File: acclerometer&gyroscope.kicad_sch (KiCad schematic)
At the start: 5 parts, among them U11 LSM6DS3

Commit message: PCB routing
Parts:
- renumbered C39 to C41, C40 to C42
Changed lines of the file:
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@@
 	(title_block
 		(title "3D Accelerometer & 3D Gyroscope")
-		(date "2025-11-26")
+		(date "2025-12-01")
 		(rev "v0.0")
 		(company "TJ71PL")
@@
 		(dnp no)
 		(fields_autoplaced yes)
-		(property "Reference" "#PWR086"
+		(property "Reference" "#PWR088"
 			(at 166.37 91.44 0)
 			(effects
@@
 			(project "Precision Clock"
 				(path "/c9a8ff63-a0d1-4125-9dd1-40fb53daf536/83e9a93f-b32e-4175-81a6-6f58261db903"
-					(reference "#PWR086")
+					(reference "#PWR088")
 					(unit 1)
 				)
@@
 		(dnp no)
 		(fields_autoplaced yes)
-		(property "Reference" "#PWR082"
+		(property "Reference" "#PWR084"
 			(at 128.27 73.66 0)
 			(effects
@@
 			(project "Precision Clock"
 				(path "/c9a8ff63-a0d1-4125-9dd1-40fb53daf536/83e9a93f-b32e-4175-81a6-6f58261db903"
-					(reference "#PWR082")
+					(reference "#PWR084")
 					(unit 1)
 				)
@@
 		(dnp no)
 		(fields_autoplaced yes)
-		(property "Reference" "C40"
+		(property "Reference" "C42"
 			(at 116.84 77.4699 0)
 			(effects
@@
 			(project "Precision Clock"
 				(path "/c9a8ff63-a0d1-4125-9dd1-40fb53daf536/83e9a93f-b32e-4175-81a6-6f58261db903"
-					(reference "C40")
+					(reference "C42")
 					(unit 1)
 				)
@@
 		(dnp no)
 		(fields_autoplaced yes)
-		(property "Reference" "#PWR081"
+		(property "Reference" "#PWR083"
 			(at 113.03 91.44 0)
 			(effects
@@
 			(project "Precision Clock"
 				(path "/c9a8ff63-a0d1-4125-9dd1-40fb53daf536/83e9a93f-b32e-4175-81a6-6f58261db903"
-					(reference "#PWR081")
+					(reference "#PWR083")
 					(unit 1)
 				)
@@
 		(dnp no)
 		(fields_autoplaced yes)
-		(property "Reference" "#PWR085"
+		(property "Reference" "#PWR087"
 			(at 158.75 121.92 0)
 			(effects
@@
 			(project "Precision Clock"
 				(path "/c9a8ff63-a0d1-4125-9dd1-40fb53daf536/83e9a93f-b32e-4175-81a6-6f58261db903"
-					(reference "#PWR085")
+					(reference "#PWR087")
 					(unit 1)
 				)
@@
 		(dnp no)
 		(fields_autoplaced yes)
-		(property "Reference" "C39"
+		(property "Reference" "C41"
 			(at 104.14 77.4699 0)
 			(effects
@@
 			(project "Precision Clock"
 				(path "/c9a8ff63-a0d1-4125-9dd1-40fb53daf536/83e9a93f-b32e-4175-81a6-6f58261db903"
-					(reference "C39")
+					(reference "C41")
 					(unit 1)
 				)
@@
 		(dnp no)
 		(fields_autoplaced yes)
-		(property "Reference" "#PWR080"
+		(property "Reference" "#PWR082"
 			(at 100.33 91.44 0)
 			(effects
@@
 			(project "Precision Clock"
 				(path "/c9a8ff63-a0d1-4125-9dd1-40fb53daf536/83e9a93f-b32e-4175-81a6-6f58261db903"
-					(reference "#PWR080")
+					(reference "#PWR082")
 					(unit 1)
 				)
@@
 		(dnp no)
 		(fields_autoplaced yes)
-		(property "Reference" "#PWR083"
+		(property "Reference" "#PWR085"
 			(at 130.81 135.89 0)
 			(effects
@@
 			(project "Precision Clock"
 				(path "/c9a8ff63-a0d1-4125-9dd1-40fb53daf536/83e9a93f-b32e-4175-81a6-6f58261db903"
-					(reference "#PWR083")
+					(reference "#PWR085")
 					(unit 1)
 				)
@@
 		(dnp no)
 		(fields_autoplaced yes)
-		(property "Reference" "#PWR084"
+		(property "Reference" "#PWR086"
 			(at 153.67 105.41 0)
 			(effects
@@
 			(project "Precision Clock"
 				(path "/c9a8ff63-a0d1-4125-9dd1-40fb53daf536/83e9a93f-b32e-4175-81a6-6f58261db903"
-					(reference "#PWR084")
+					(reference "#PWR086")
 					(unit 1)
 				)

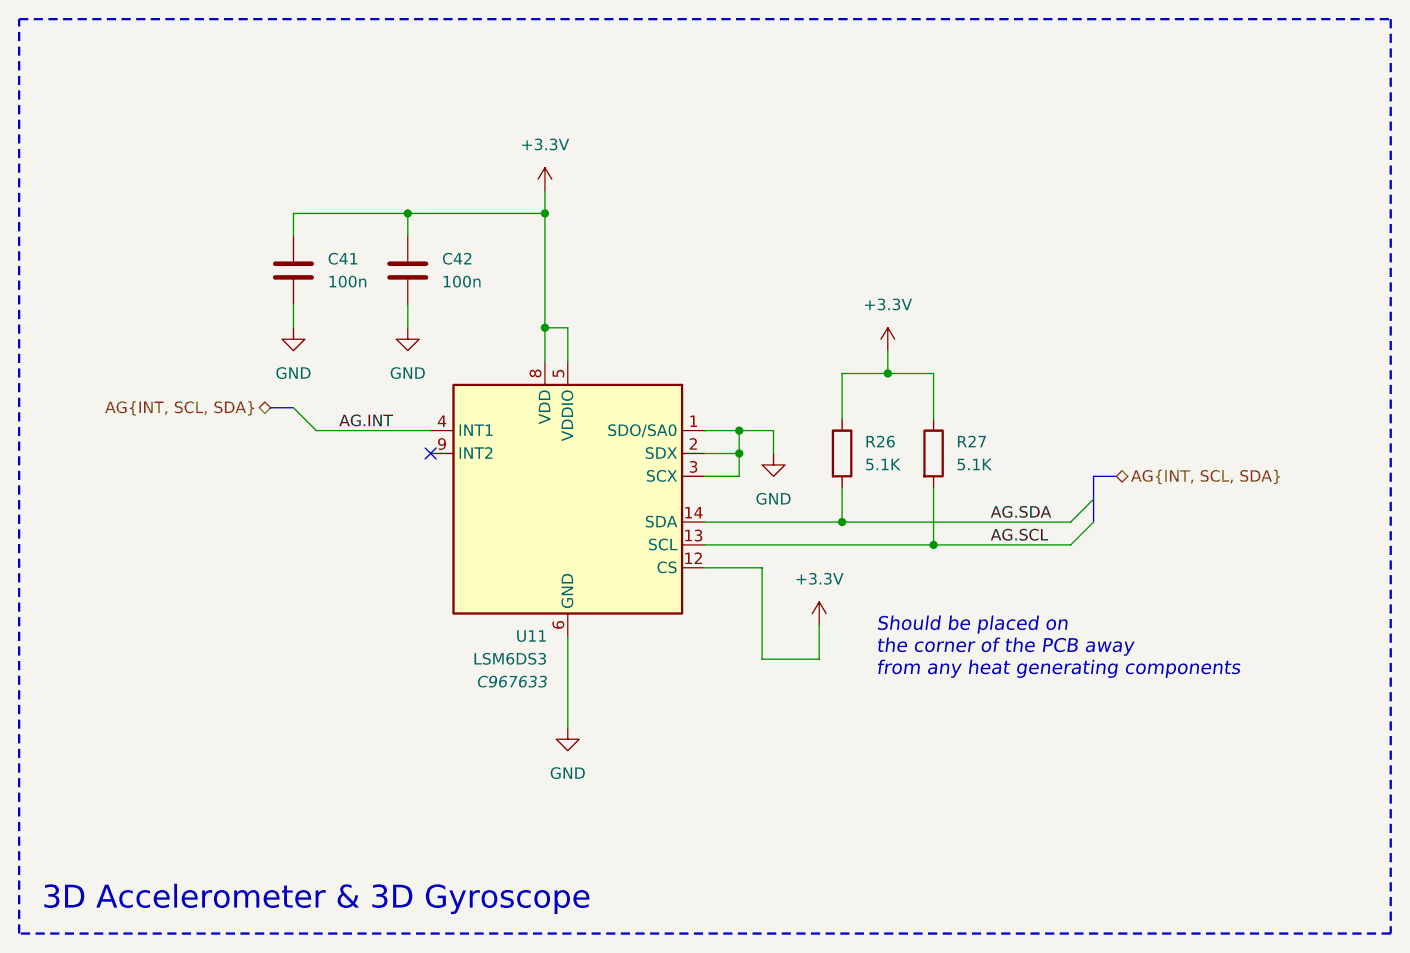
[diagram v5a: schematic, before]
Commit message: Schematic changes
- signal for dots are removed.
- power supply upgraded to buck converters.
- individually addressable Colon LEDs.
- second millisecond dot separator signal is not connected.
- buzzer can now be connected to PWM or DAC outputs.
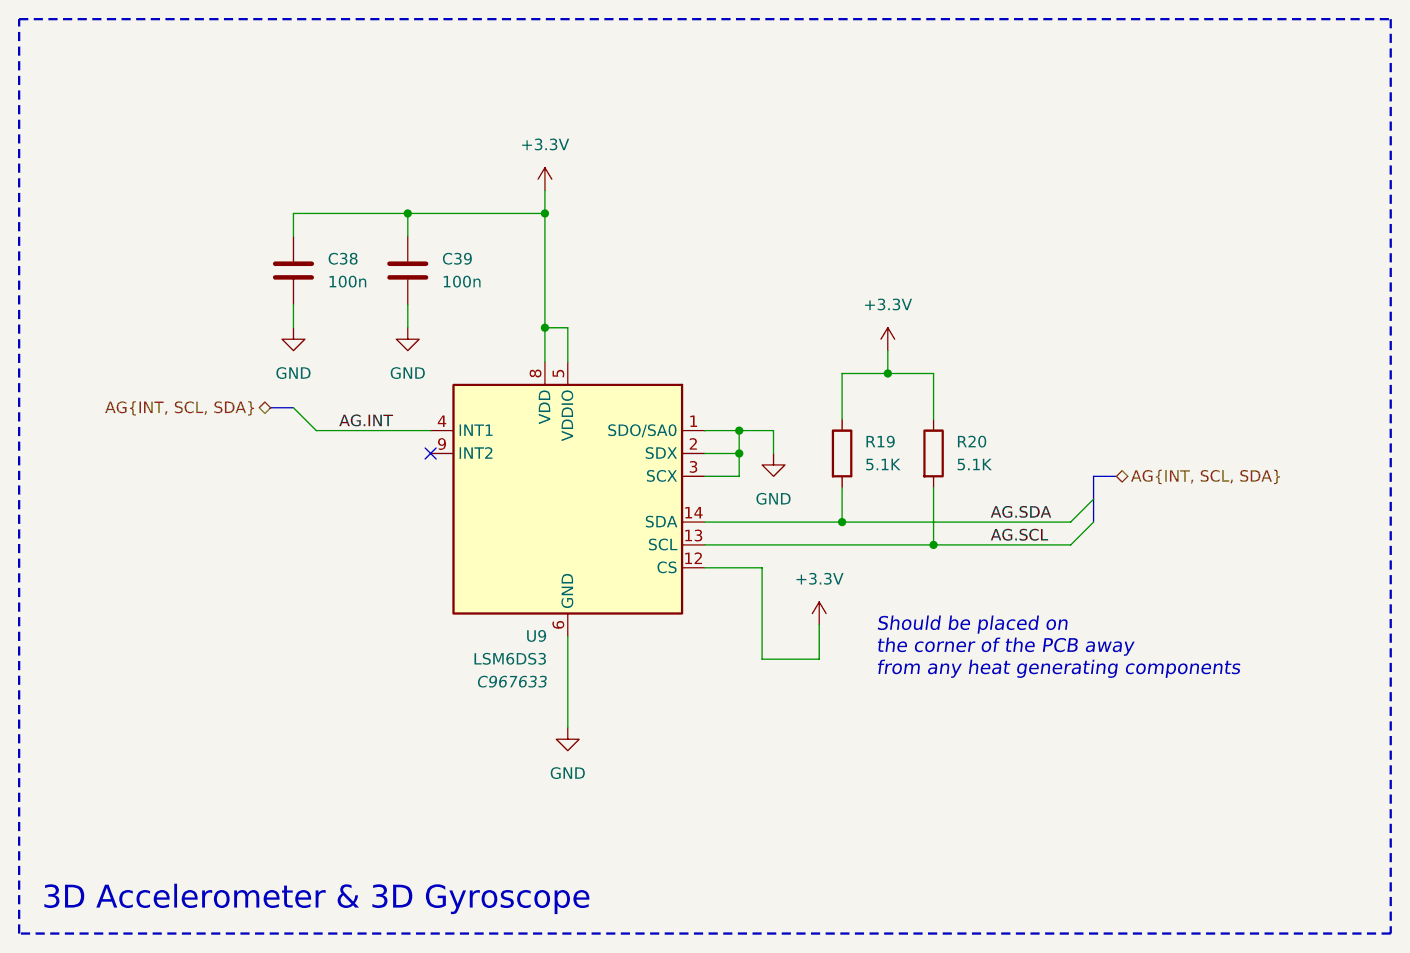
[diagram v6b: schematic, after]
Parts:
- renumbered C41 to C38, C42 to C39, R26 to R19, R27 to R20, U11 to U9
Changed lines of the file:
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@@
 	(title_block
 		(title "3D Accelerometer & 3D Gyroscope")
-		(date "2025-12-01")
+		(date "2025-12-23")
 		(rev "v0.0")
 		(company "TJ71PL")
@@
 		(dnp no)
 		(fields_autoplaced yes)
-		(property "Reference" "R26"
+		(property "Reference" "R19"
 			(at 163.83 97.7899 0)
 			(effects
@@
 			(project "Precision Clock"
 				(path "/c9a8ff63-a0d1-4125-9dd1-40fb53daf536/83e9a93f-b32e-4175-81a6-6f58261db903"
-					(reference "R26")
+					(reference "R19")
 					(unit 1)
 				)
@@
 		(dnp no)
 		(fields_autoplaced yes)
-		(property "Reference" "R27"
+		(property "Reference" "R20"
 			(at 173.99 97.7899 0)
 			(effects
@@
 			(project "Precision Clock"
 				(path "/c9a8ff63-a0d1-4125-9dd1-40fb53daf536/83e9a93f-b32e-4175-81a6-6f58261db903"
-					(reference "R27")
+					(reference "R20")
 					(unit 1)
 				)
@@
 		(dnp no)
 		(fields_autoplaced yes)
-		(property "Reference" "#PWR088"
+		(property "Reference" "#PWR074"
 			(at 166.37 91.44 0)
 			(effects
@@
 			(project "Precision Clock"
 				(path "/c9a8ff63-a0d1-4125-9dd1-40fb53daf536/83e9a93f-b32e-4175-81a6-6f58261db903"
-					(reference "#PWR088")
+					(reference "#PWR074")
 					(unit 1)
 				)
@@
 		(dnp no)
 		(fields_autoplaced yes)
-		(property "Reference" "#PWR084"
+		(property "Reference" "#PWR070"
 			(at 128.27 73.66 0)
 			(effects
@@
 			(project "Precision Clock"
 				(path "/c9a8ff63-a0d1-4125-9dd1-40fb53daf536/83e9a93f-b32e-4175-81a6-6f58261db903"
-					(reference "#PWR084")
+					(reference "#PWR070")
 					(unit 1)
 				)
@@
 		(on_board yes)
 		(dnp no)
-		(property "Reference" "U11"
+		(property "Reference" "U9"
 			(at 128.524 119.38 0)
 			(effects
@@
 			(project "Precision Clock"
 				(path "/c9a8ff63-a0d1-4125-9dd1-40fb53daf536/83e9a93f-b32e-4175-81a6-6f58261db903"
-					(reference "U11")
+					(reference "U9")
 					(unit 1)
 				)
@@
 		(dnp no)
 		(fields_autoplaced yes)
-		(property "Reference" "C42"
+		(property "Reference" "C39"
 			(at 116.84 77.4699 0)
 			(effects
@@
 			(project "Precision Clock"
 				(path "/c9a8ff63-a0d1-4125-9dd1-40fb53daf536/83e9a93f-b32e-4175-81a6-6f58261db903"
-					(reference "C42")
+					(reference "C39")
 					(unit 1)
 				)
@@
 		(dnp no)
 		(fields_autoplaced yes)
-		(property "Reference" "#PWR083"
+		(property "Reference" "#PWR069"
 			(at 113.03 91.44 0)
 			(effects
@@
 			(project "Precision Clock"
 				(path "/c9a8ff63-a0d1-4125-9dd1-40fb53daf536/83e9a93f-b32e-4175-81a6-6f58261db903"
-					(reference "#PWR083")
+					(reference "#PWR069")
 					(unit 1)
 				)
@@
 		(dnp no)
 		(fields_autoplaced yes)
-		(property "Reference" "#PWR087"
+		(property "Reference" "#PWR073"
 			(at 158.75 121.92 0)
 			(effects
@@
 			(project "Precision Clock"
 				(path "/c9a8ff63-a0d1-4125-9dd1-40fb53daf536/83e9a93f-b32e-4175-81a6-6f58261db903"
-					(reference "#PWR087")
+					(reference "#PWR073")
 					(unit 1)
 				)
@@
 		(dnp no)
 		(fields_autoplaced yes)
-		(property "Reference" "C41"
+		(property "Reference" "C38"
 			(at 104.14 77.4699 0)
 			(effects
@@
 			(project "Precision Clock"
 				(path "/c9a8ff63-a0d1-4125-9dd1-40fb53daf536/83e9a93f-b32e-4175-81a6-6f58261db903"
-					(reference "C41")
+					(reference "C38")
 					(unit 1)
 				)
@@
 		(dnp no)
 		(fields_autoplaced yes)
-		(property "Reference" "#PWR082"
+		(property "Reference" "#PWR068"
 			(at 100.33 91.44 0)
 			(effects
@@
 			(project "Precision Clock"
 				(path "/c9a8ff63-a0d1-4125-9dd1-40fb53daf536/83e9a93f-b32e-4175-81a6-6f58261db903"
-					(reference "#PWR082")
+					(reference "#PWR068")
 					(unit 1)
 				)
@@
 		(dnp no)
 		(fields_autoplaced yes)
-		(property "Reference" "#PWR085"
+		(property "Reference" "#PWR071"
 			(at 130.81 135.89 0)
 			(effects
@@
 			(project "Precision Clock"
 				(path "/c9a8ff63-a0d1-4125-9dd1-40fb53daf536/83e9a93f-b32e-4175-81a6-6f58261db903"
-					(reference "#PWR085")
+					(reference "#PWR071")
 					(unit 1)
 				)
@@
 		(dnp no)
 		(fields_autoplaced yes)
-		(property "Reference" "#PWR086"
+		(property "Reference" "#PWR072"
 			(at 153.67 105.41 0)
 			(effects
@@
 			(project "Precision Clock"
 				(path "/c9a8ff63-a0d1-4125-9dd1-40fb53daf536/83e9a93f-b32e-4175-81a6-6f58261db903"
-					(reference "#PWR086")
+					(reference "#PWR072")
 					(unit 1)
 				)

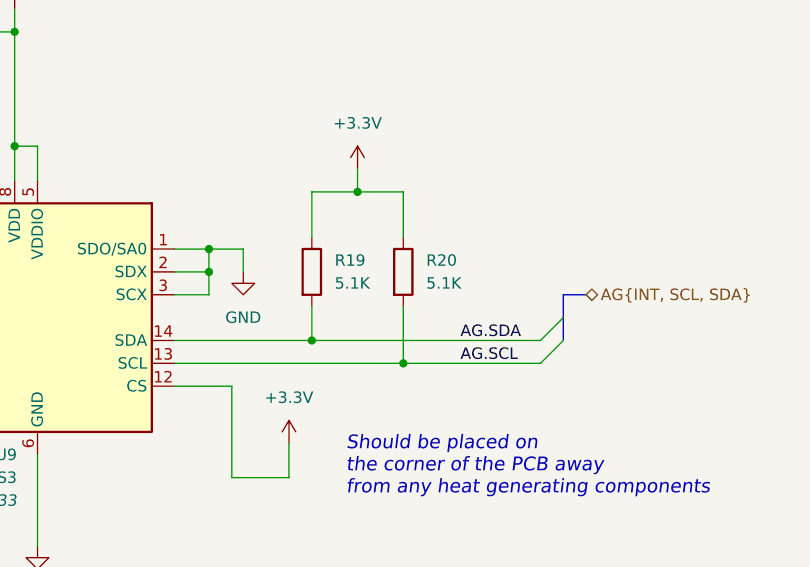
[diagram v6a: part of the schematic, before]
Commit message: Power stage changes
- removal of potentiometer
- addition of rotary encoder
- addition of ambient light sensor
- addition of unity gain differential amplifier.
- reording of the schematic.
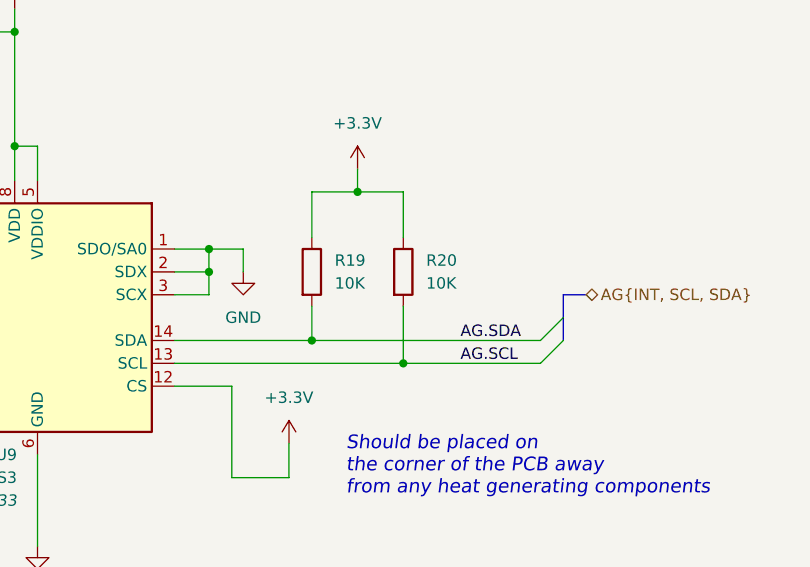
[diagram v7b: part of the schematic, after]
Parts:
- R19, R20: value 5.1K -> 10K
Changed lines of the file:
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@@
 			)
 		)
-		(property "Value" "5.1K"
+		(property "Value" "10K"
 			(at 163.83 100.3299 0)
 			(effects
@@
 			)
 		)
-		(property "Value" "5.1K"
+		(property "Value" "10K"
 			(at 173.99 100.3299 0)
 			(effects

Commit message: updated power
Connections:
- net +3.3V: no longer C38.1, C39.1, U9.5 (VDDIO), U9.8 (VDD)
- new net +3V0: C38.1, C39.1, U9.5 (VDDIO), U9.8 (VDD)
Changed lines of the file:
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@@
 	(title_block
 		(title "3D Accelerometer & 3D Gyroscope")
-		(date "2025-12-23")
+		(date "2026-01-23")
 		(rev "v0.0")
 		(company "TJ71PL")
@@
 	)
 	(symbol
-		(lib_id "power:+3.3V")
-		(at 128.27 69.85 0)
-		(mirror y)
-		(unit 1)
-		(exclude_from_sim no)
-		(in_bom yes)
-		(on_board yes)
-		(dnp no)
-		(fields_autoplaced yes)
-		(property "Reference" "#PWR070"
-			(at 128.27 73.66 0)
-			(effects
-				(font
-					(size 1.27 1.27)
-				)
-				(hide yes)
-			)
-		)
-		(property "Value" "+3.3V"
-			(at 128.27 64.77 0)
-			(effects
-				(font
-					(size 1.27 1.27)
-				)
-			)
-		)
-		(property "Footprint" ""
-			(at 128.27 69.85 0)
-			(effects
-				(font
-					(size 1.27 1.27)
-				)
-				(hide yes)
-			)
-		)
-		(property "Datasheet" ""
-			(at 128.27 69.85 0)
-			(effects
-				(font
-					(size 1.27 1.27)
-				)
-				(hide yes)
-			)
-		)
-		(property "Description" "Power symbol creates a global label with name \"+3.3V\""
-			(at 128.27 69.85 0)
-			(effects
-				(font
-					(size 1.27 1.27)
-				)
-				(hide yes)
-			)
-		)
-		(pin "1"
-		)
-		(instances
-			(project "Precision Clock"
-				(path "/c9a8ff63-a0d1-4125-9dd1-40fb53daf536/83e9a93f-b32e-4175-81a6-6f58261db903"
-					(reference "#PWR070")
-					(unit 1)
-				)
-			)
-		)
-	)
-	(symbol
 		(lib_id "Sensor_Motion:LSM6DS3")
 		(at 130.81 104.14 0)
@@
 					(unit 1)
 				)
+			)
+		)
+	)
+	(symbol
+		(lib_id "power:+3V0")
+		(at 128.27 69.85 0)
+		(unit 1)
+		(exclude_from_sim no)
+		(in_bom yes)
+		(on_board yes)
+		(dnp no)
+		(fields_autoplaced yes)
+		(property "Reference" "#PWR054"
+			(at 128.27 73.66 0)
+			(effects
+				(font
+					(size 1.27 1.27)
+				)
+				(hide yes)
+			)
+		)
+		(property "Value" "+3V0"
+			(at 128.27 64.77 0)
+			(effects
+				(font
+					(size 1.27 1.27)
+				)
+			)
+		)
+		(property "Footprint" ""
+			(at 128.27 69.85 0)
+			(effects
+				(font
+					(size 1.27 1.27)
+				)
+				(hide yes)
+			)
+		)
+		(property "Datasheet" ""
+			(at 128.27 69.85 0)
+			(effects
+				(font
+					(size 1.27 1.27)
+				)
+				(hide yes)
+			)
+		)
+		(property "Description" "Power symbol creates a global label with name \"+3V0\""
+			(at 128.27 69.85 0)
+			(effects
+				(font
+					(size 1.27 1.27)
+				)
+				(hide yes)
+			)
+		)
+		(pin "1"
+		)
+		(instances
+			(project "Precision Clock"
+				(path "/c9a8ff63-a0d1-4125-9dd1-40fb53daf536/83e9a93f-b32e-4175-81a6-6f58261db903"
+					(reference "#PWR054")
+					(unit 1)
+				)
